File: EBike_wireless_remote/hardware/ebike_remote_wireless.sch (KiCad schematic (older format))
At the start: 6 parts

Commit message: Updated schematics
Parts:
- removed U?: nRF52840 USB Dongle, symbol Dongle:nRF52840
- removed coin_cell: CR2032, symbol Device:Battery_Cell
- added J?: Bootloader flash, symbol Connector_Generic:Conn_01x03
- added U?: Nordic nRF52840 USB Dongle, symbol Wireless_eBike:Nordic_nRF52840_USB_Dongle
- added coincell: CR2032 coin cell, symbol Device:Battery_Cell
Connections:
- net at button_4.2: now also U?.7 (P1.15)
- net at button_3.2: now also U?.8 (P1.13)
- net at button_2.2: now also U?.9 (P1.10)
- net at button_1.2: now also U?.10 (P0.13)
- net at button_1.1, button_2.1, button_3.1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: now also U?.1 (VBUS)
- new net: U?.2 (VDD_out), coincell.1 (+)
- new net: U?.3 (P0.09), coincell.2 (-)
- no-connect marks 11 -> 13
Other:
- note added: "Connector to flash the bootloader.\nYou will need it only once, so you\ncan remove the wires after flashing."
- note added: "should work for\nat least 2 years"
- note removed: "flash firmware\nonly needed\none time"
- note removed: "hopefully will\nlast 1 year"
- moved on the sheet: button_1, button_2, button_3, button_4
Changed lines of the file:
@@
 Comment4 ""
 $EndDescr
-NoConn ~ 7050 2950
-Text Label 7550 3050 0    60   ~ 0
-GND
-Text Label 7550 3150 0    60   ~ 0
-RST
-Text Label 7550 3250 0    60   ~ 0
-SWDCLK
-Text Label 7550 3350 0    60   ~ 0
-SWDIO
 NoConn ~ 3800 8100
-$Comp
-L Dongle:nRF52840 U?
-U 1 1 5EEB15B7
-P 6500 3450
-F 0 "U?" H 6500 3500 60  0000 C CNN
-F 1 "nRF52840 USB Dongle" H 6500 2900 60  0000 C CNB
-F 2 "" H 6500 3450 60  0000 C CNN
-F 3 "" H 6500 3450 60  0000 C CNN
-	1    6500 3450
-	1    0    0    -1
-$EndComp
-Wire Wire Line
-	7050 3050 7550 3050
-Wire Wire Line
-	7050 3150 7550 3150
-Wire Wire Line
-	7050 3250 7550 3250
-Wire Wire Line
-	7050 3350 7550 3350
-NoConn ~ 7050 3450
-NoConn ~ 7050 3550
-NoConn ~ 7050 3650
-NoConn ~ 7050 3750
-NoConn ~ 7050 3850
-NoConn ~ 5950 3850
-NoConn ~ 5950 3750
-NoConn ~ 5950 3050
-NoConn ~ 5950 3250
-$Comp
-L Device:Battery_Cell coin_cell
-U 1 1 5F4A3162
-P 5300 2950
-F 0 "coin_cell" V 5150 3000 50  0000 C CNN
-F 1 "CR2032" V 5050 3000 50  0000 C CNB
-F 2 "" V 5300 3010 50  0001 C CNN
-F 3 "~" V 5300 3010 50  0001 C CNN
-	1    5300 2950
-	0    1    1    0
-$EndComp
 $Comp
 L Switch:SW_Push button_1
 U 1 1 5F4A3714
-P 3750 2750
-F 0 "button_1" H 3750 2950 50  0000 C CNN
-F 1 "UP" H 3750 3050 50  0000 C CNB
-F 2 "" H 3750 2950 50  0001 C CNN
-F 3 "~" H 3750 2950 50  0001 C CNN
-	1    3750 2750
-	1    0    0    -1
-$EndComp
+P 2650 3000
+F 0 "button_1" H 2650 3200 50  0000 C CNN
+F 1 "UP" H 2650 3300 50  0000 C CNB
+F 2 "" H 2650 3200 50  0001 C CNN
+F 3 "~" H 2650 3200 50  0001 C CNN
+	1    2650 3000
+	1    0    0    -1
+$EndComp
+Wire Wire Line
+	2300 3000 2450 3000
+Wire Wire Line
+	3150 3900 4050 3900
+Connection ~ 2300 4000
+Wire Wire Line
+	2300 4000 2450 4000
+$Comp
+L Switch:SW_Push button_3
+U 1 1 5F4A4B3B
+P 2650 4000
+F 0 "button_3" H 2650 4200 50  0000 C CNN
+F 1 "ENTER" H 2650 4300 50  0000 C CNB
+F 2 "" H 2650 4200 50  0001 C CNN
+F 3 "~" H 2650 4200 50  0001 C CNN
+	1    2650 4000
+	1    0    0    -1
+$EndComp
+Connection ~ 2300 3500
+Wire Wire Line
+	2300 4000 2300 3500
+Wire Wire Line
+	2300 3500 2300 3000
+Wire Wire Line
+	2300 3500 2450 3500
+$Comp
+L Switch:SW_Push button_2
+U 1 1 5F4A3F33
+P 2650 3500
+F 0 "button_2" H 2650 3700 50  0000 C CNN
+F 1 "DOWN" H 2650 3800 50  0000 C CNB
+F 2 "" H 2650 3700 50  0001 C CNN
+F 3 "~" H 2650 3700 50  0001 C CNN
+	1    2650 3500
+	1    0    0    -1
+$EndComp
+Wire Wire Line
+	2850 4000 3000 4000
+Wire Wire Line
+	3000 4000 3000 3800
+Wire Wire Line
+	3000 3800 4050 3800
+Wire Wire Line
+	4050 3700 3000 3700
+Wire Wire Line
+	3000 3700 3000 3500
+Wire Wire Line
+	3000 3500 2850 3500
+Wire Wire Line
+	2850 3000 3150 3000
+Wire Wire Line
+	3150 3000 3150 3600
+Wire Wire Line
+	3150 3600 4050 3600
+Wire Notes Line
+	2150 2550 3500 2550
+Wire Notes Line
+	3500 2550 3500 4800
+Wire Notes Line
+	3500 4800 2150 4800
+Wire Notes Line
+	2150 2550 2150 4800
+Text Notes 4250 2900 0    79   ~ 0
+(wireless board)
+Text Notes 7550 3450 0    79   ~ 0
+Connector to flash the bootloader.\nYou will need it only once, so you\ncan remove the wires after flashing.
+Text Notes 2350 2500 0    79   ~ 0
+VLCD5 handlebar\nremote keypad
+$Comp
+L Wireless_eBike:Nordic_nRF52840_USB_Dongle U?
+U 1 1 600AD575
+P 4750 3950
+F 0 "U?" H 4750 4987 60  0001 C CNN
+F 1 "Nordic nRF52840 USB Dongle" H 4750 4900 60  0000 C CNN
+F 2 "" H 4600 3800 60  0000 C CNN
+F 3 "" H 4600 3800 60  0000 C CNN
+	1    4750 3950
+	1    0    0    -1
+$EndComp
+Wire Notes Line
+	6000 4050 6000 3400
+Wire Notes Line
+	6000 3400 6750 3400
+Text Notes 5900 3350 0    79   ~ 0
+should work for\nat least 2 years
+$Comp
+L Device:Battery_Cell coincell
+U 1 1 600B4826
+P 6450 3800
+F 0 "coincell" V 6300 3850 50  0001 C CNN
+F 1 "CR2032 coin cell" H 6380 4130 50  0000 C CNN
+F 2 "" V 6450 3860 50  0001 C CNN
+F 3 "~" V 6450 3860 50  0001 C CNN
+	1    6450 3800
+	1    0    0    -1
+$EndComp
+Wire Wire Line
+	2850 4500 3150 4500
+Wire Wire Line
+	2300 4500 2300 4000
+Wire Wire Line
+	3150 4500 3150 3900
+Wire Wire Line
+	2450 4500 2300 4500
 $Comp
 L Switch:SW_Push button_4
 U 1 1 5F4A4B45
-P 3750 4250
-F 0 "button_4" H 3750 4450 50  0000 C CNN
-F 1 "POWER" H 3750 4550 50  0000 C CNB
-F 2 "" H 3750 4450 50  0001 C CNN
-F 3 "~" H 3750 4450 50  0001 C CNN
-	1    3750 4250
-	1    0    0    -1
-$EndComp
-Wire Wire Line
-	5500 2950 5950 2950
-Wire Wire Line
-	5150 3150 5150 2950
-Wire Wire Line
-	5150 2950 5200 2950
-Wire Wire Line
-	3550 4250 3400 4250
-Wire Wire Line
-	3400 2750 3550 2750
-Wire Wire Line
-	4250 4250 4250 3650
-Wire Wire Line
-	4250 3650 5950 3650
-Connection ~ 3400 3750
-Wire Wire Line
-	3400 4250 3400 3750
-Wire Wire Line
-	3400 3750 3550 3750
-$Comp
-L Switch:SW_Push button_3
-U 1 1 5F4A4B3B
-P 3750 3750
-F 0 "button_3" H 3750 3950 50  0000 C CNN
-F 1 "ENTER" H 3750 4050 50  0000 C CNB
-F 2 "" H 3750 3950 50  0001 C CNN
-F 3 "~" H 3750 3950 50  0001 C CNN
-	1    3750 3750
-	1    0    0    -1
-$EndComp
-Connection ~ 3400 3250
-Wire Wire Line
-	3400 3750 3400 3250
-Wire Wire Line
-	3400 3250 3400 2750
-Wire Wire Line
-	3400 3250 3550 3250
-$Comp
-L Switch:SW_Push button_2
-U 1 1 5F4A3F33
-P 3750 3250
-F 0 "button_2" H 3750 3450 50  0000 C CNN
-F 1 "DOWN" H 3750 3550 50  0000 C CNB
-F 2 "" H 3750 3450 50  0001 C CNN
-F 3 "~" H 3750 3450 50  0001 C CNN
-	1    3750 3250
-	1    0    0    -1
-$EndComp
-Wire Wire Line
-	3950 3750 4100 3750
-Wire Wire Line
-	4100 3750 4100 3550
-Wire Wire Line
-	4100 3550 5950 3550
-Wire Wire Line
-	5950 3450 4100 3450
-Wire Wire Line
-	4100 3450 4100 3250
-Wire Wire Line
-	4100 3250 3950 3250
-Wire Wire Line
-	3950 4250 4250 4250
-Wire Wire Line
-	3950 2750 4250 2750
-Wire Wire Line
-	4250 2750 4250 3350
-Wire Wire Line
-	3400 2750 3400 2150
-Wire Wire Line
-	3400 2150 4450 2150
-Wire Wire Line
-	4450 2150 4450 3150
-Wire Wire Line
-	4450 3150 5150 3150
-Connection ~ 3400 2750
-Connection ~ 5150 3150
-Wire Wire Line
-	5150 3150 5950 3150
-Wire Wire Line
-	4250 3350 5950 3350
-Wire Notes Line
-	3250 2000 4600 2000
-Wire Notes Line
-	4600 2000 4600 4400
-Wire Notes Line
-	4600 4400 3250 4400
-Wire Notes Line
-	3250 2000 3250 4400
-Wire Notes Line
-	5050 3250 5050 2600
-Wire Notes Line
-	5050 2600 5600 2600
-Wire Notes Line
-	5600 2600 5600 3250
-Wire Notes Line
-	5600 3250 5050 3250
-Text Notes 6000 4200 0    79   ~ 0
-(wireless board)
-Text Notes 7950 3350 0    79   ~ 0
-flash firmware\nonly needed\none time
-Text Notes 4950 2550 0    79   ~ 0
-hopefully will\nlast 1 year
-Text Notes 3450 1950 0    79   ~ 0
-VLCD5 handlebar\nremote keypad
+P 2650 4500
+F 0 "button_4" H 2650 4700 50  0000 C CNN
+F 1 "POWER" H 2650 4800 50  0000 C CNB
+F 2 "" H 2650 4700 50  0001 C CNN
+F 3 "~" H 2650 4700 50  0001 C CNN
+	1    2650 4500
+	1    0    0    -1
+$EndComp
+Wire Wire Line
+	2300 4500 2300 4650
+Wire Wire Line
+	2300 4650 3350 4650
+Wire Wire Line
+	3350 4650 3350 4500
+Wire Wire Line
+	3350 4500 4050 4500
+Connection ~ 2300 4500
+Wire Notes Line
+	6750 3400 6750 4050
+Wire Notes Line
+	6000 4050 6750 4050
+NoConn ~ 4050 4000
+NoConn ~ 4050 4100
+NoConn ~ 4050 4200
+NoConn ~ 4050 4300
+NoConn ~ 4050 4400
+NoConn ~ 5450 4400
+NoConn ~ 5450 4300
+NoConn ~ 5450 4200
+NoConn ~ 5450 4100
+NoConn ~ 5450 4000
+NoConn ~ 5450 3900
+Text Label 7550 3700 0    60   ~ 0
+GND
+Text Label 7550 3900 0    60   ~ 0
+SWDIO
+Text Label 7550 3800 0    60   ~ 0
+SWDCLK
+Text Label 5750 3450 2    60   ~ 0
+SWDCLK
+Text Label 5750 4500 2    60   ~ 0
+GND
+Text Label 3850 3450 0    60   ~ 0
+SWDIO
+Wire Notes Line style solid rgb(255, 114, 0)
+	4200 3450 3850 3450
+Wire Notes Line style solid rgb(255, 114, 0)
+	5750 3450 5300 3450
+Wire Notes Line style solid rgb(255, 114, 0)
+	5750 4500 5450 4500
+Wire Notes Line style solid rgb(255, 114, 0)
+	7950 3700 7550 3700
+Wire Notes Line style solid rgb(255, 114, 0)
+	7950 3800 7550 3800
+Wire Notes Line style solid rgb(255, 114, 0)
+	7950 3900 7550 3900
+Wire Wire Line
+	5450 3800 6250 3800
+Wire Wire Line
+	6250 3700 6250 3550
+Wire Wire Line
+	6250 3550 6450 3550
+Wire Wire Line
+	6450 3550 6450 3600
+Wire Wire Line
+	5450 3700 6250 3700
+Wire Wire Line
+	6250 3800 6250 3950
+Wire Wire Line
+	6250 3950 6450 3950
+Wire Wire Line
+	6450 3950 6450 3900
+$Comp
+L Connector_Generic:Conn_01x03 J?
+U 1 1 600C2D4C
+P 8150 3800
+F 0 "J?" H 8230 3842 50  0001 L CNN
+F 1 "Bootloader flash" V 8300 3450 50  0000 L CNN
+F 2 "" H 8150 3800 50  0001 C CNN
+F 3 "~" H 8150 3800 50  0001 C CNN
+	1    8150 3800
+	1    0    0    -1
+$EndComp
+NoConn ~ 5450 3600
 $EndSCHEMATC

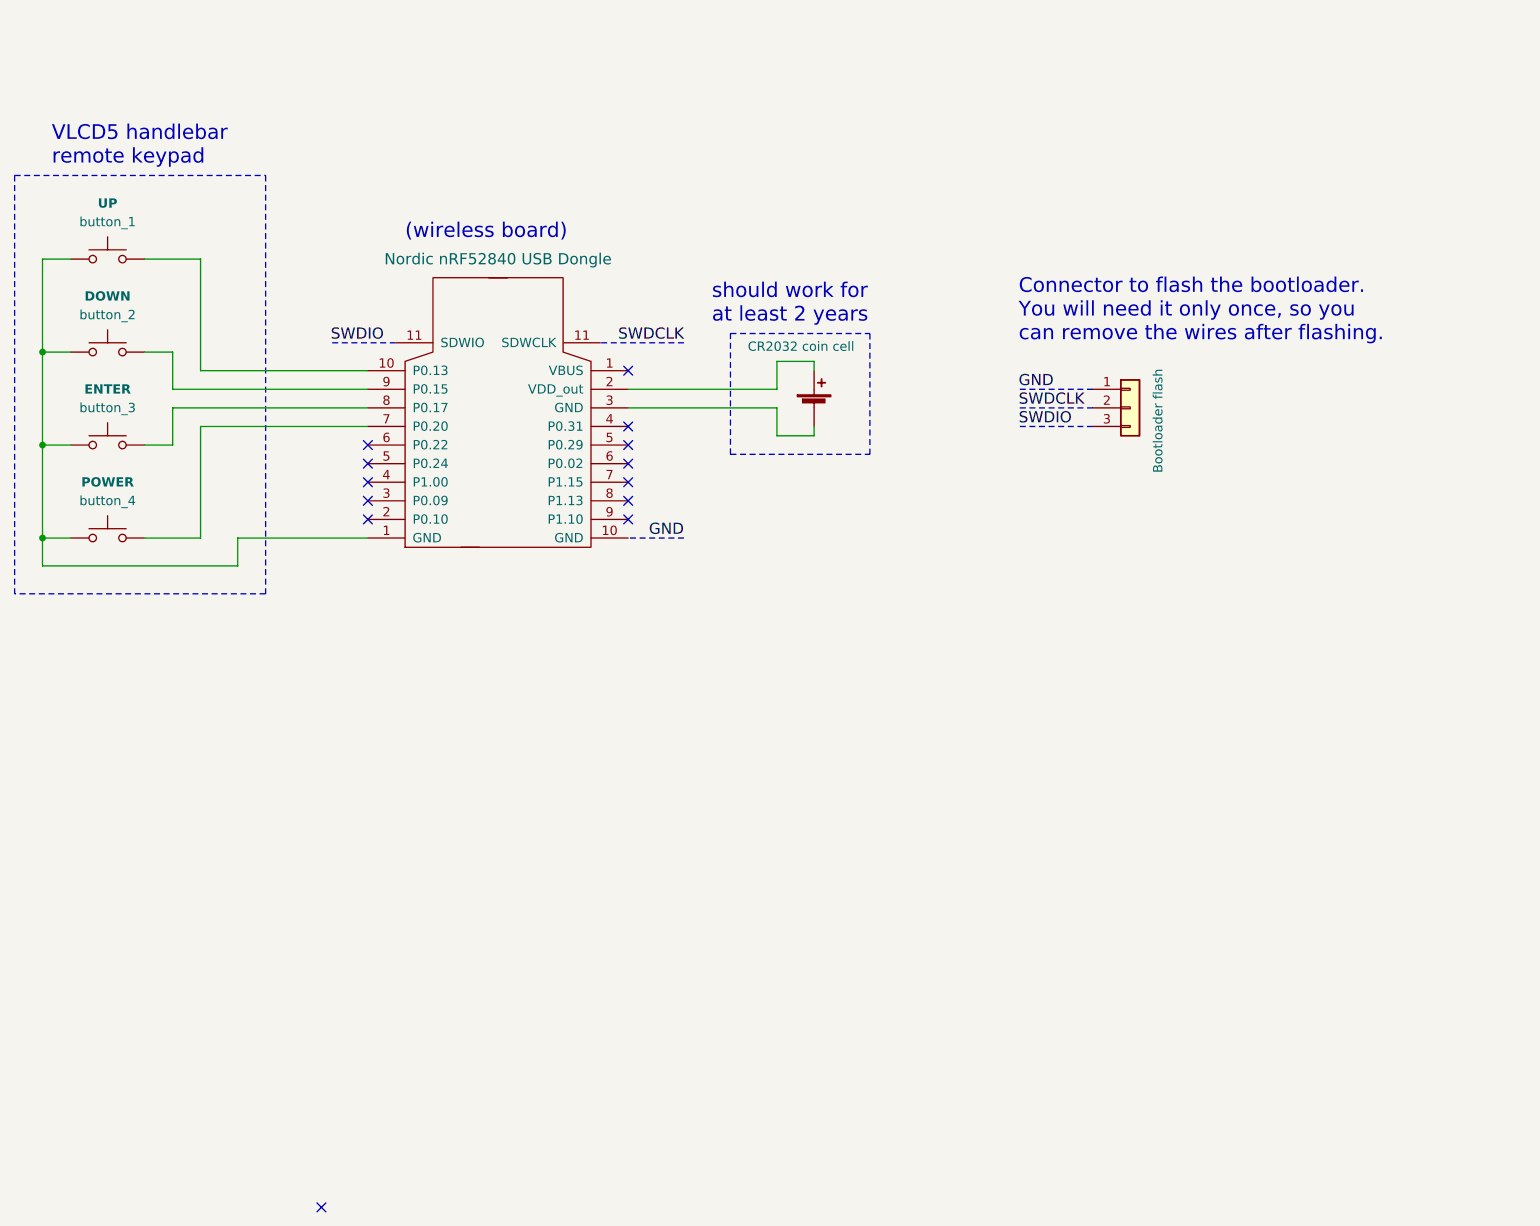
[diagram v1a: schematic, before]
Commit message: Updated schematic for the TSDZ2 wireless board and remote, removing the bootloader flash
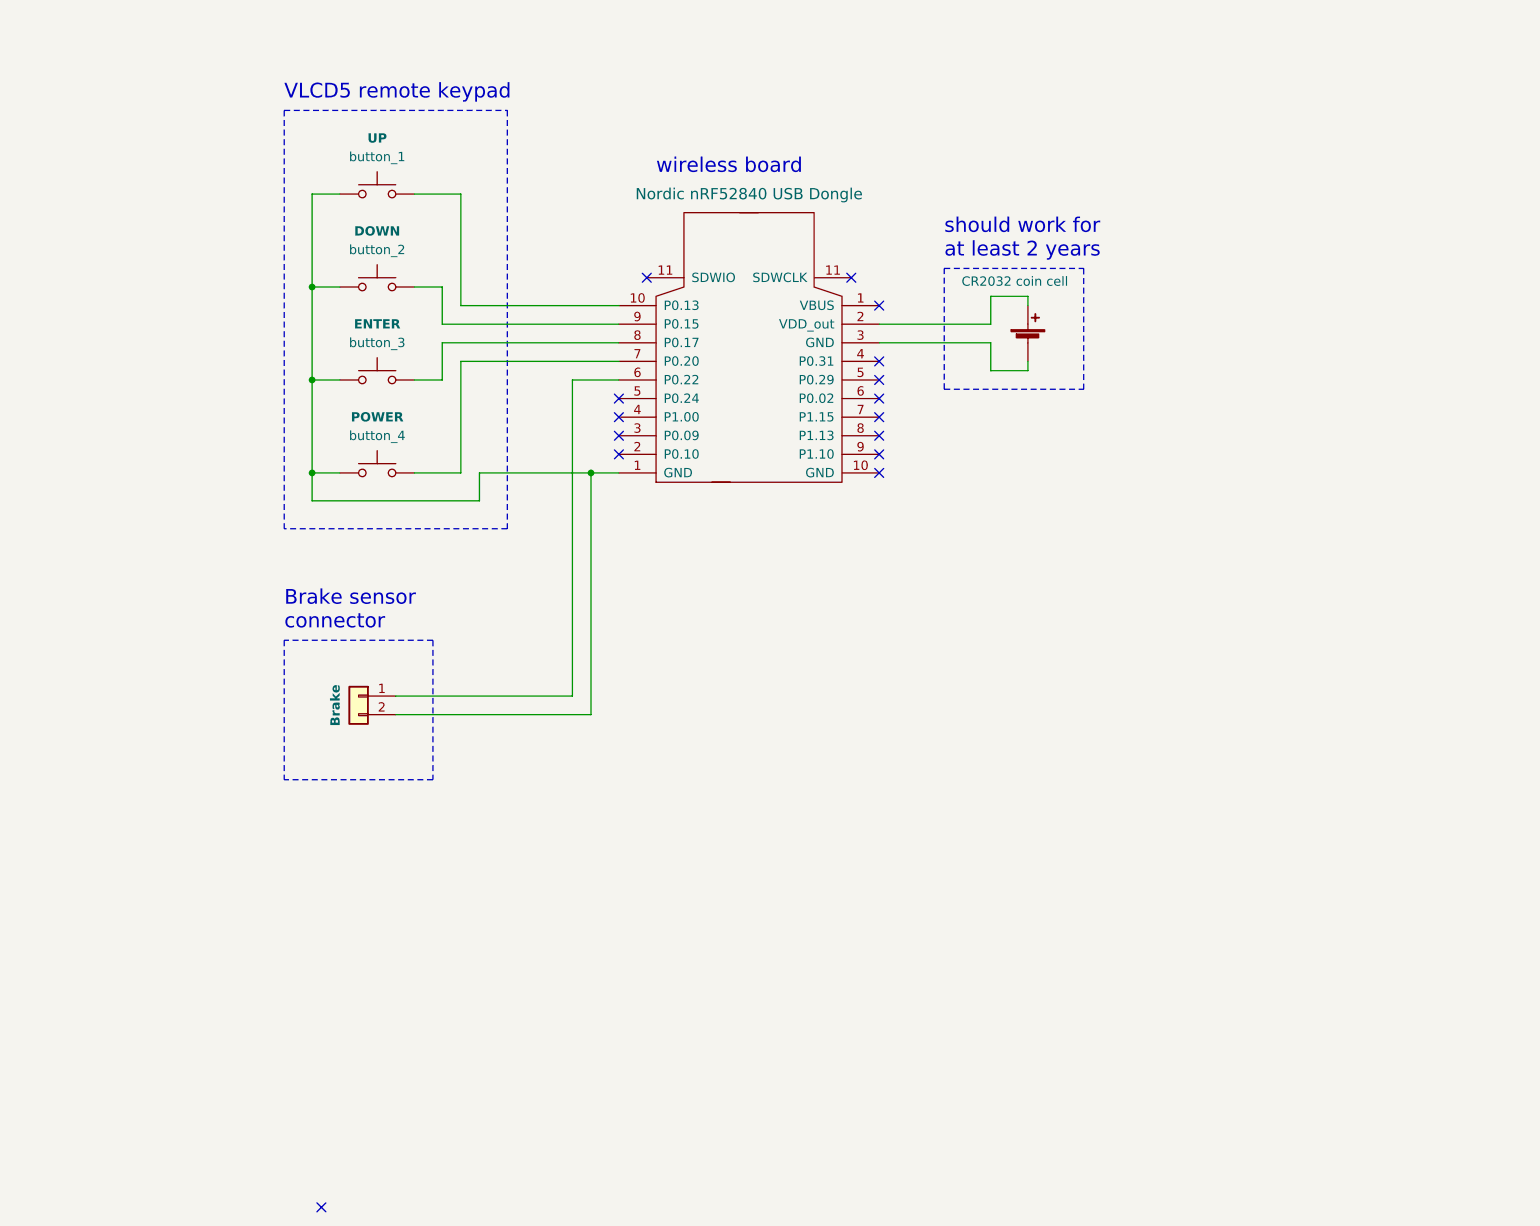
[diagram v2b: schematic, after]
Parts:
- removed J?: Bootloader flash, symbol Connector_Generic:Conn_01x03
- added J?: Brake, symbol Connector_Generic:Conn_01x02
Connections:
- net at U?.1 (VBUS), button_1.1, button_2.1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: now also J?.2 (Pin_2)
- net at U?.2 (VDD_out): now also coincell.1 (+)
- net at U?.3 (P0.09): now also coincell.2 (-)
- net at U?.6 (P0.22): now also J?.1 (Pin_1)
- no-connect marks 13 -> 15
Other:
- note added: "Brake sensor\nconnector"
- note added: "VLCD5 remote keypad"
- note added: "wireless board"
- note removed: "(wireless board)"
- note removed: "Connector to flash the bootloader.\nYou will need it only once, so you\ncan remove the wires after flashing."
- note removed: "VLCD5 handlebar\nremote keypad"
- moved on the sheet: button_1, button_2, button_3, button_4
